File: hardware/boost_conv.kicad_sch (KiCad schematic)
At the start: 11 parts, among them U1 TPS61288

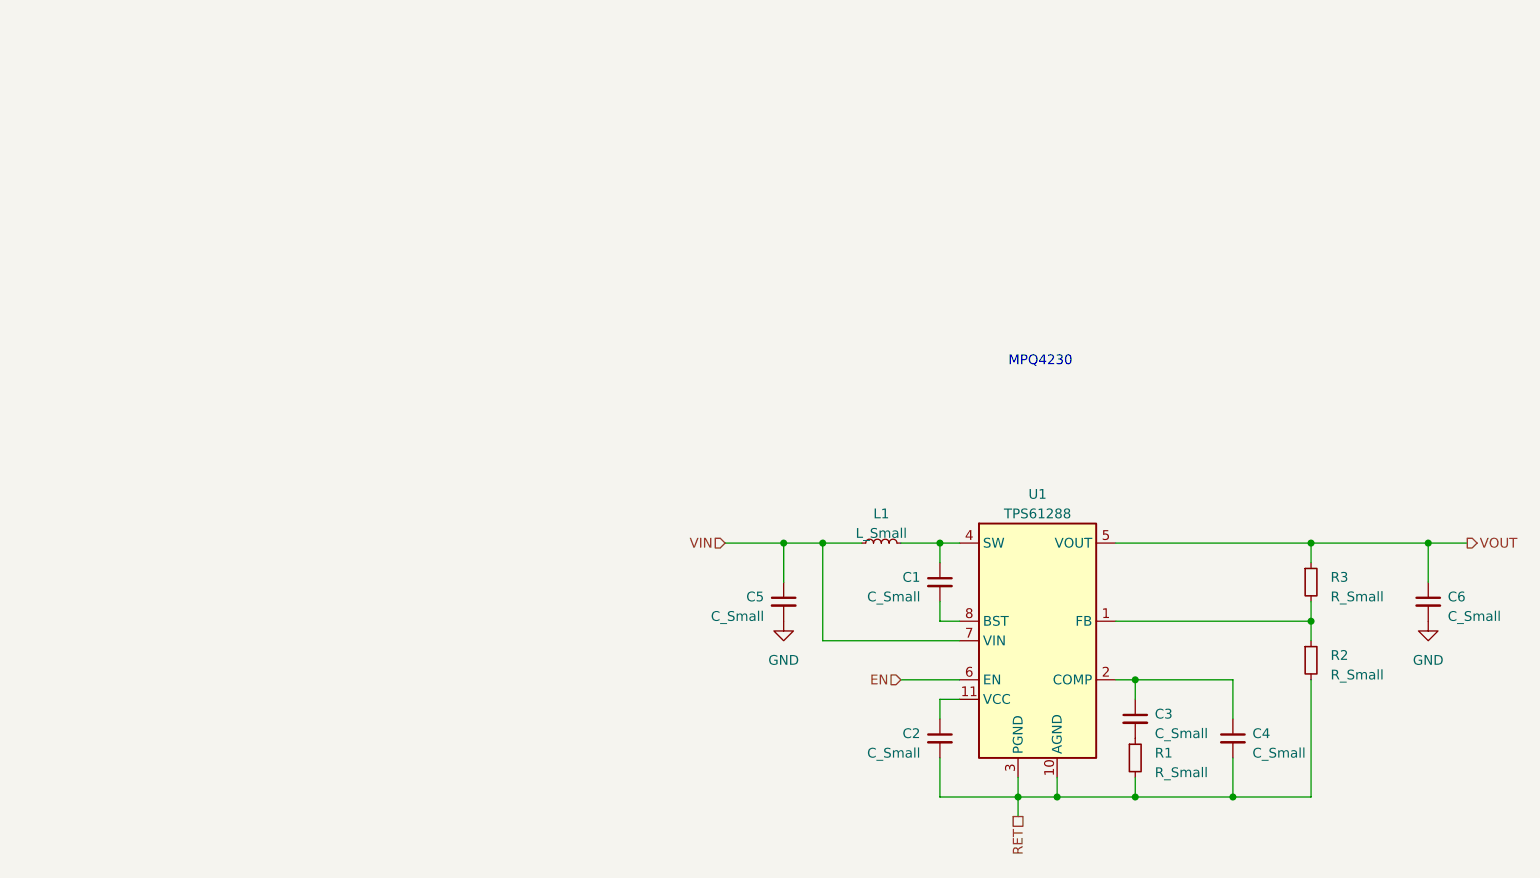
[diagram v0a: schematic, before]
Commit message: Added BMS and DC/DC
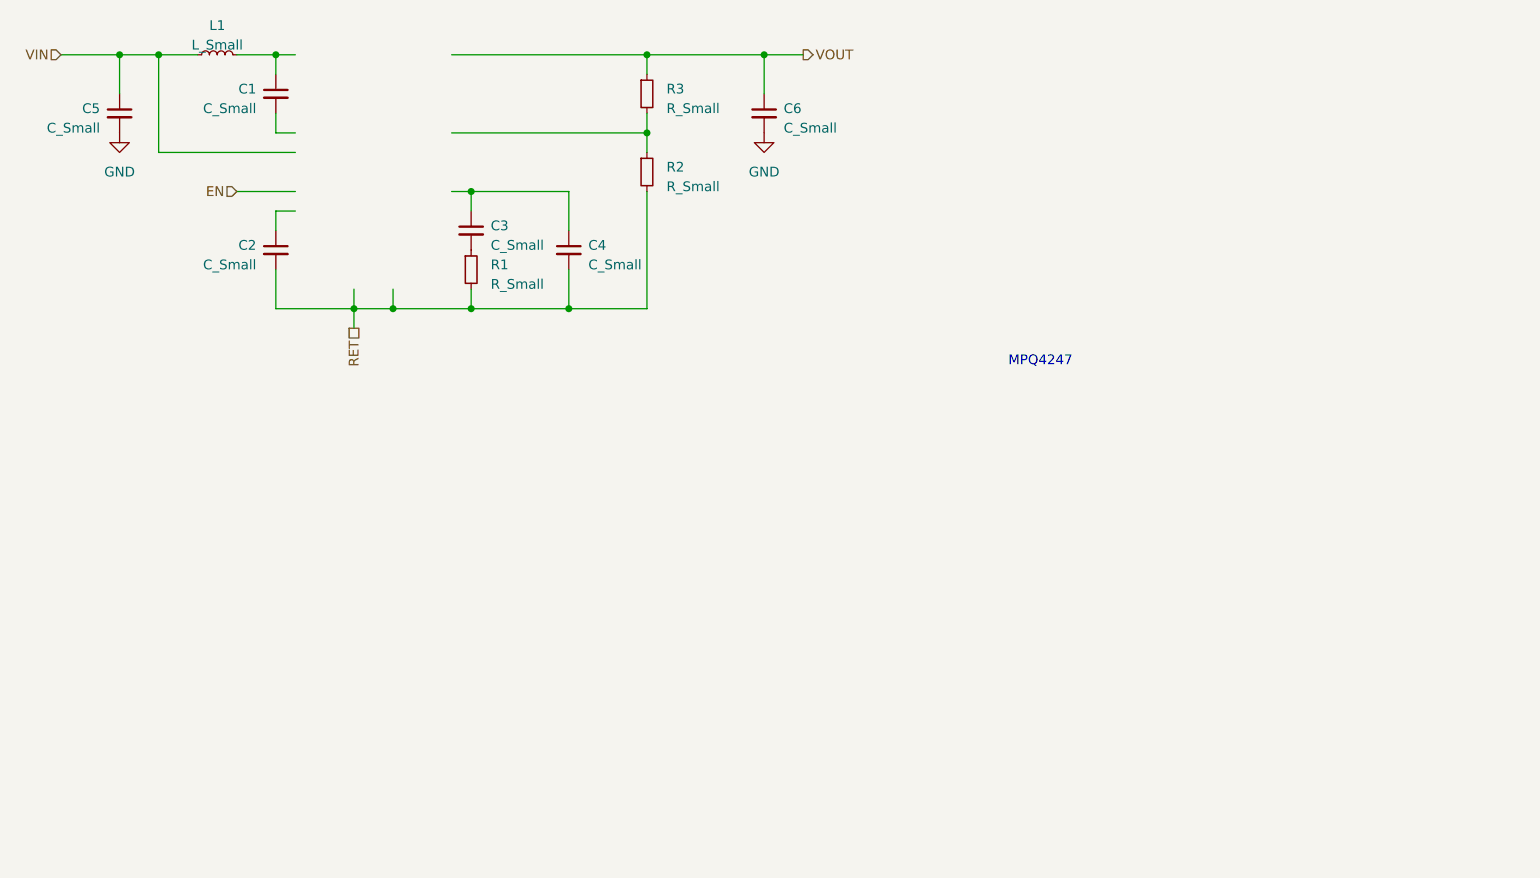
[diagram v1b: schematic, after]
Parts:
- removed U1: TPS61288, Package_DFN_QFN:Texas_VQFN-HR_RQQ0011A, symbol Regulator_Switching:TPS61288
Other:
- note added: "MPQ4247"
- note removed: "MPQ4230"
- moved on the sheet: C1, C2, C3, C4, C5, C6, L1, R1, R2, R3
